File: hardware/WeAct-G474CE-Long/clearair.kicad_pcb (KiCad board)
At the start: 2 copper layers, 116.6 x 58.4 mm, 35 parts, among them J3 SPS30 wire header (1 VDD, 2 S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, J4 BME680 wire header (1 VCC, 2 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, J5 MQ131 wire header (1 VCC, 2 G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, J6 MiCS-4514 wire header (1 VCC,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, J7 RTC PCF8563, M2 80mm fan front, M3 80mm fan rear, Q1 2N7000, Q2 2N7000, Q3 2N2222A, SW1 RESET, SW2 COLD_BOOT, U5 RobotDyn AC dimmer

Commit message: fix layout and script generators
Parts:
- SW1: value RESET -> RESET red; footprint Button_Switch_THT:SW_PUSH_6mm -> SW_Tactile_3x6_2pin
- SW2: value COLD_BOOT -> COLD_BOOT white; footprint Button_Switch_THT:SW_PUSH_6mm -> SW_Tactile_3x6_2pin
- moved SW2 9.60 mm to (201.6, 71.2)
- moved R9 3.53 mm to (152.6, 102.5)
- moved R12 2.06 mm to (134.8, 102.5)
- moved BZ1 1.45 mm to (157.6, 97.4)
- moved SW1 1.25 mm to (201.2, 78.8)
- moved Q3 1.10 mm to (142.4, 97.4)
- moved PS1 1.08 mm to (219.1, 71.3)
- moved R14 0.94 mm to (201.3, 101.8)
- moved R10 0.81 mm to (114.5, 102.5)
- moved R11 0.81 mm to (119.5, 102.5)
- moved R13 0.81 mm to (137.3, 102.5)
- moved Q1 0.81 mm to (106.8, 97.4)
- moved Q2 0.81 mm to (124.6, 97.4)
- moved J3 0.78 mm to (152.6, 77.1)
- moved J5 0.76 mm to (106.8, 77.1)
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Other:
- board size 116.6 x 58.4 mm -> 117.3 x 58.4 mm

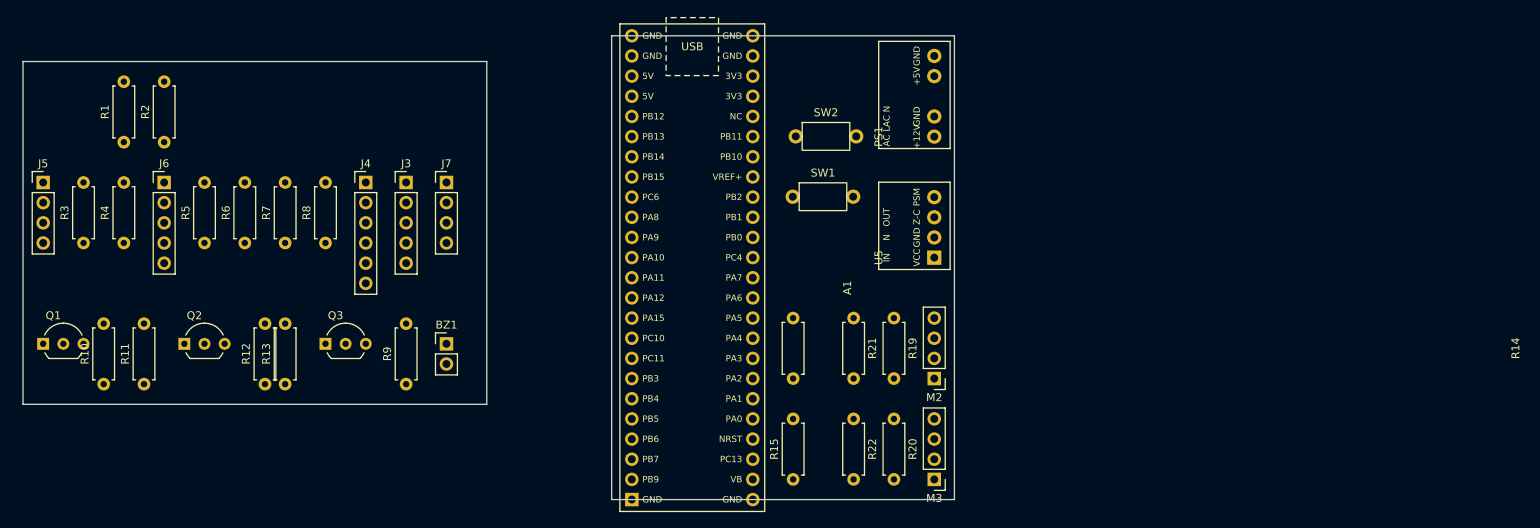
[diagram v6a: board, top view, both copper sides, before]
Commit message: fix script generators to not need external json files, source is now PCB and SCH
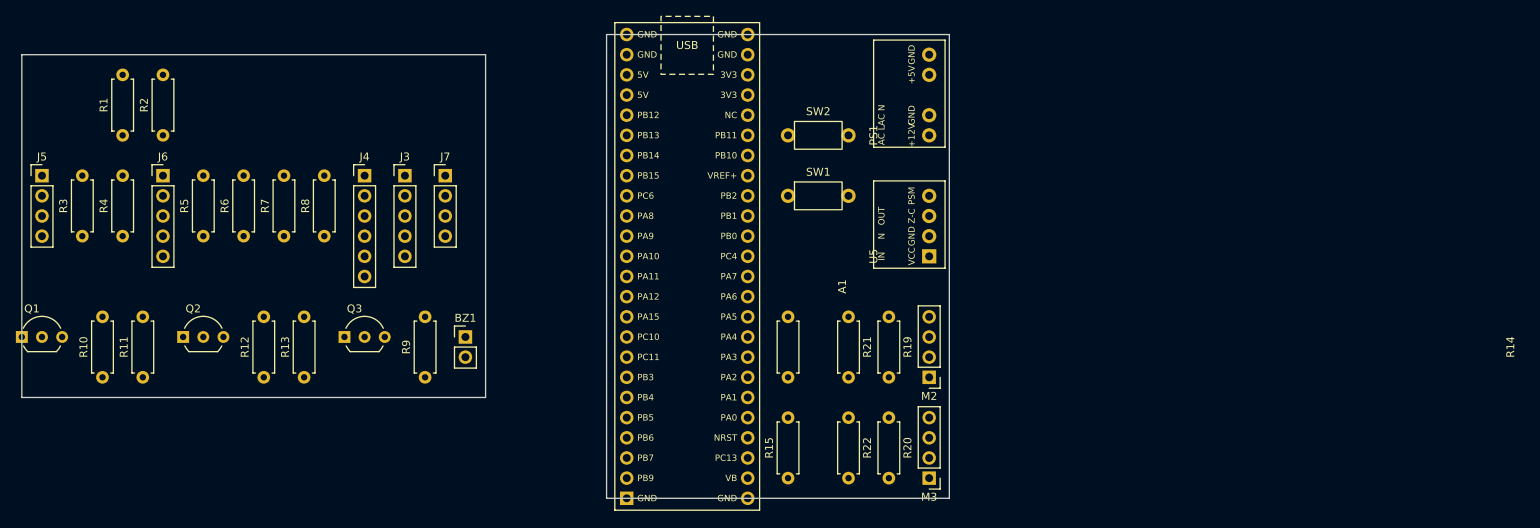
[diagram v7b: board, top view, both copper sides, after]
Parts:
- J3: value SPS30 wire header (1 VDD, 2 SDA, 3 SCL, 4 SEL, 5 GND) -> SPS30
- J4: value BME680 wire header (1 VCC, 2 GND, 3 SCL, 4 SDA, 5 SDO, 6 CS) -> BME680
- J5: value MQ131 wire header (1 VCC, 2 GND, 3 DO nc, 4 AO) -> MQ131
- J6: value MiCS-4514 wire header (1 VCC, 2 GND, 3 RED, 4 NOX, 5 PRE) -> MiCS-4514
- moved Q1 2.82 mm to (104.1, 96.5)
- moved BZ1 2.54 mm to (160.0, 96.5)
- moved Q3 2.54 mm to (144.8, 96.5)
- moved R13 2.54 mm to (139.7, 101.6)
- moved R9 2.54 mm to (154.9, 101.6)
- moved SW2 0.98 mm to (200.7, 71.1)
- moved R5 0.87 mm to (127.0, 83.8)
- moved R7 0.87 mm to (137.2, 83.8)
- moved R3 0.87 mm to (111.8, 83.8)
- moved R4 0.87 mm to (116.8, 83.8)
- moved R6 0.87 mm to (132.1, 83.8)
- moved R8 0.87 mm to (142.2, 83.8)
- moved J3 0.87 mm to (152.4, 76.2)
- moved J4 0.87 mm to (147.3, 76.2)
- moved J7 0.87 mm to (157.5, 76.2)
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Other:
- board size 117.3 x 58.4 mm -> 116.8 x 58.4 mm

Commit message: cleanup & verify
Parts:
- moved R1 5.08 mm to (111.8, 71.1)
- moved R2 5.08 mm to (116.8, 71.1)
- moved Q1 3.59 mm to (106.7, 99.1), turned to 90 degrees
- moved Q2 3.59 mm to (127.0, 99.1), turned to 90 degrees
- moved Q3 3.59 mm to (147.3, 99.1), turned to 90 degrees
